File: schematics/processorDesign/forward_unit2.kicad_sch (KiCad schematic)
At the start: 8 parts

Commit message: the interrupt is now working correctly
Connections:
- net at U?.: now also U?.1
- net at U?.: now also U?.2

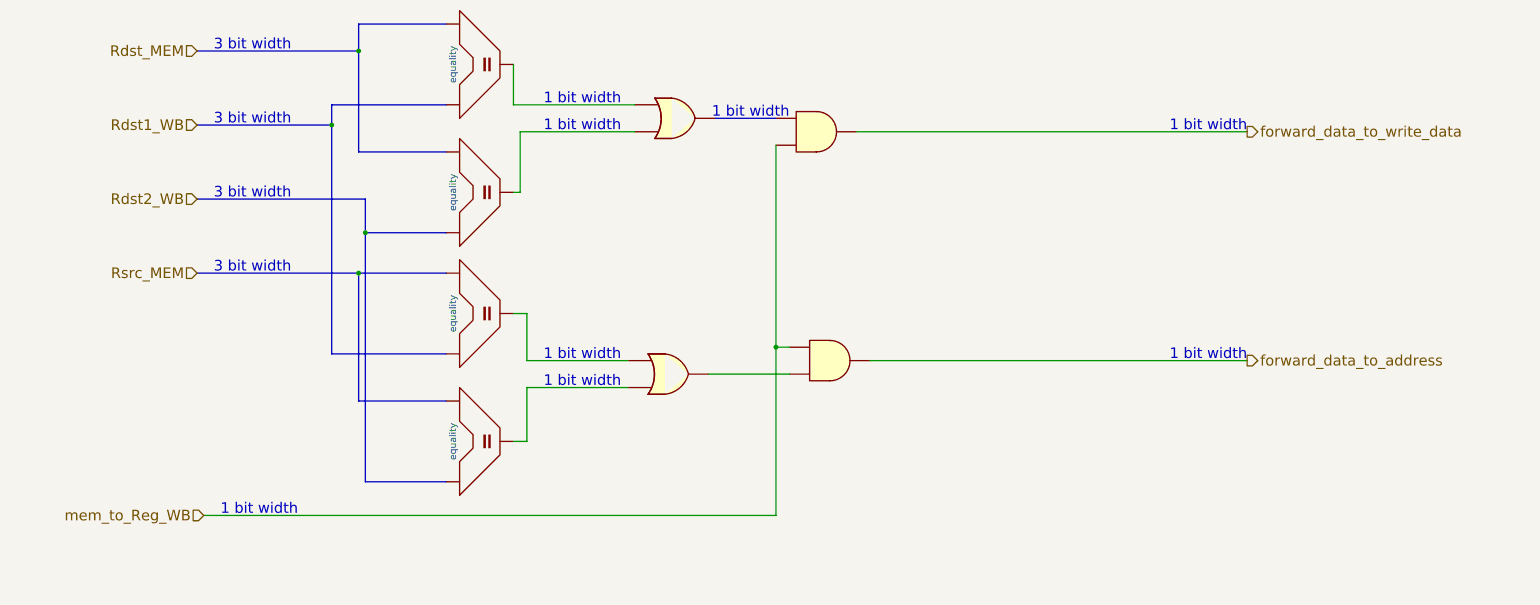
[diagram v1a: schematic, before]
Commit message: the processor is up and running tested and verified, need only tests for some bonus instructions like all I_types instruction except LDM , MUL , DIV , testing EDU and HDU
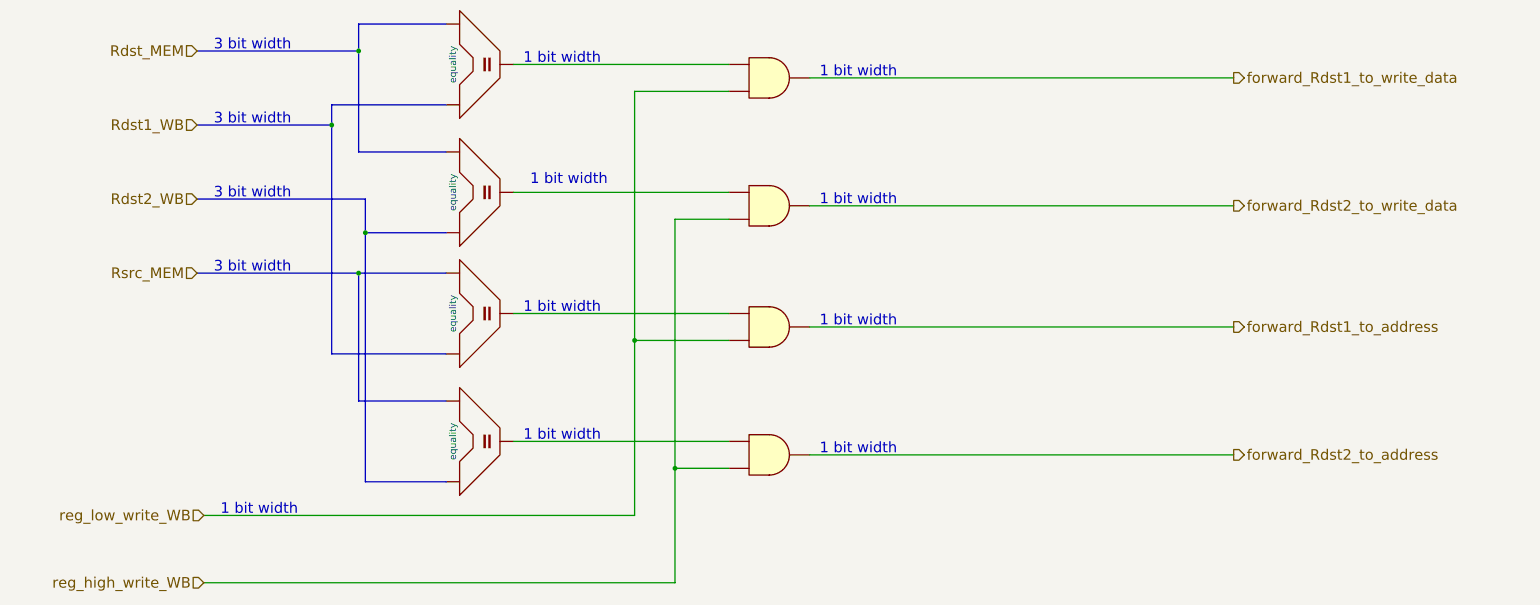
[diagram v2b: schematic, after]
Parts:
- removed U? (x2): 4071, symbol 4xxx:4071
- added U? (x2): 4081, symbol 4xxx:4081
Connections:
- net at U?.: now also U?.1 (x2)
- net at U?.1: now also U?.
- net reg_low_write_WB: now reaches U?.2
- net reg_low_write_WB: now also U?.2
- net forward_data_to_address renamed forward_Rdst1_to_address
- net forward_data_to_write_data renamed forward_Rdst1_to_write_data
- removed net mem_to_Reg_WB: U?.1, U?.2
- new net: U?., U?.1
- new net forward_Rdst2_to_address: U?.3
- new net forward_Rdst2_to_write_data: U?.3
- new net reg_high_write_WB: U?.2, U?.2

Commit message: the processor is now up and running , tested and verified , except for the part related to labels due to a bug in the assembler
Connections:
- net at U?.: now also U?.1 (x2)

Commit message: the processor is now up and running , tested and verified completly for almost most of the things
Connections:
- net at U?.: now also U?.1 (x2)

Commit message: added small code to EDU
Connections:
- net at U?.: now also U?.1 (x2)
